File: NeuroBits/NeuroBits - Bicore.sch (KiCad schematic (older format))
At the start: 8 parts, among them IC1 NL17SZ14DBVT1G, IC2 NL17SZ14DBVT1G, J1 Conn_01x04_Female

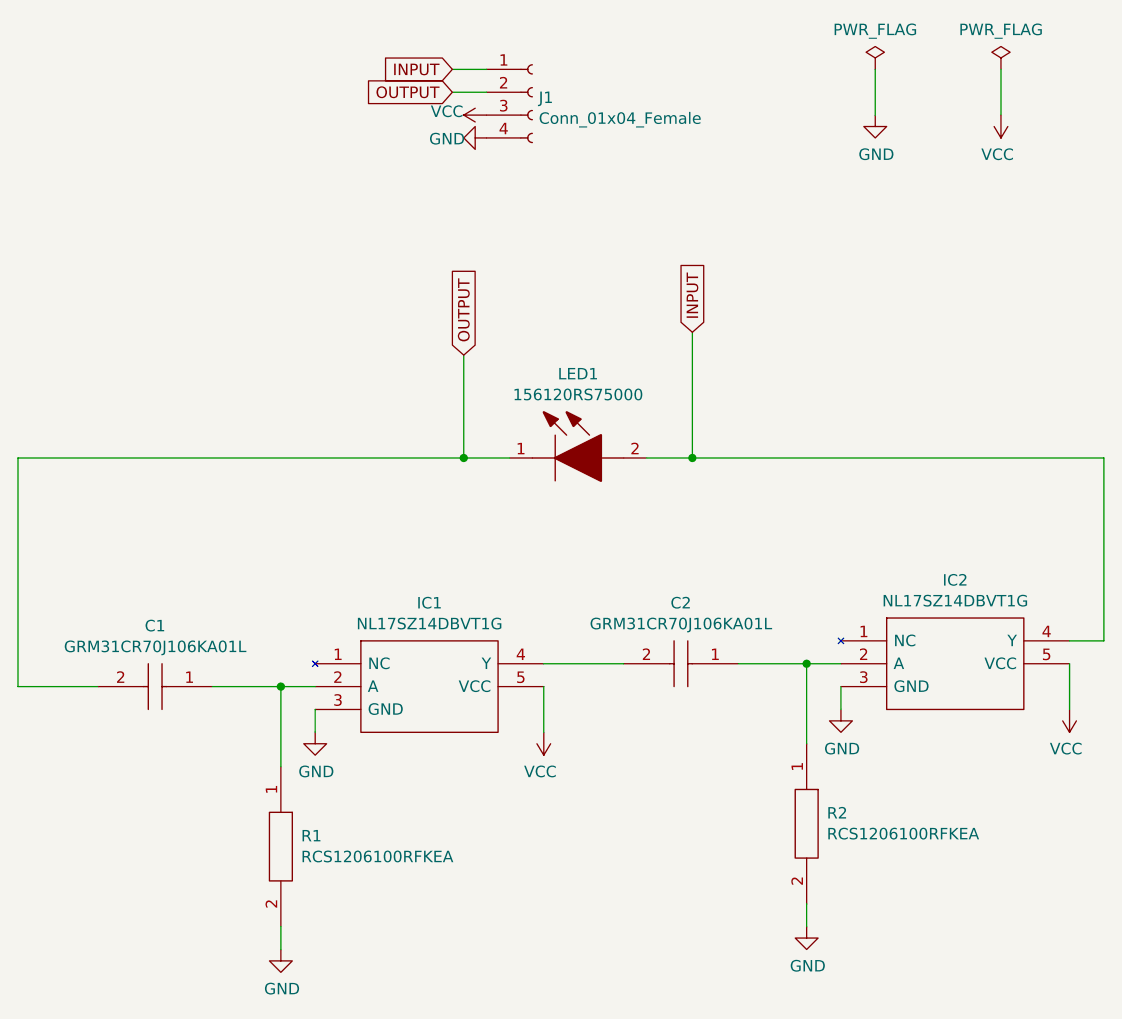
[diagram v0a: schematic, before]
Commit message: added BioRuler initial commit
added project for a custom STM32 based solar powered ultracapacitor microcontroller for biological research
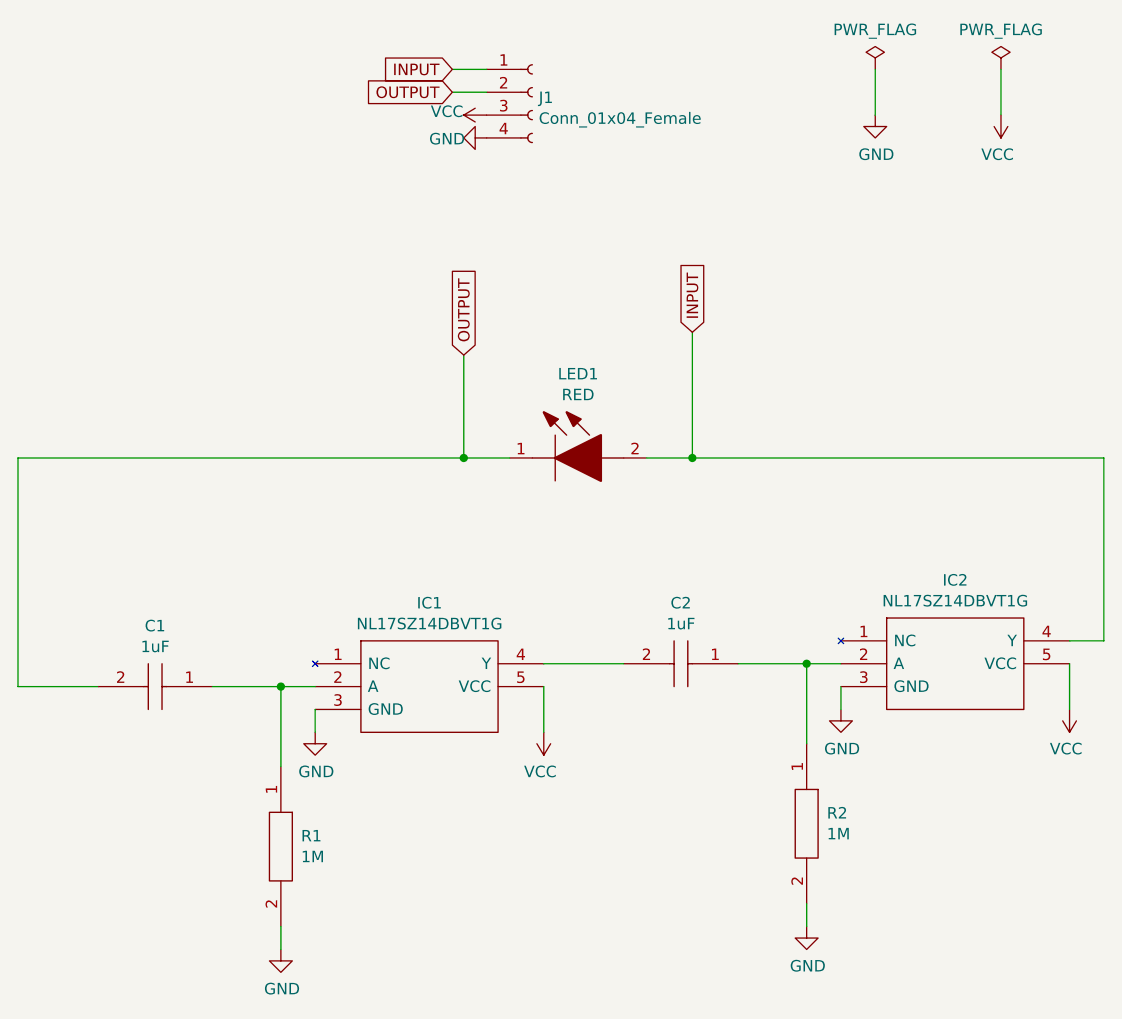
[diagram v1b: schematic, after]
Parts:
- C1, C2: value GRM31CR70J106KA01L -> 1uF
- LED1: value 156120RS75000 -> RED
- R1, R2: value RCS1206100RFKEA -> 1M
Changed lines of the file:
@@
 P 4600 4450
 F 0 "R1" V 4904 4538 50  0000 L CNN
-F 1 "RCS1206100RFKEA" V 4995 4538 50  0000 L CNN
+F 1 "1M" V 4995 4538 50  0000 L CNN
 F 2 "RESC3216X65N" H 5150 4500 50  0001 L CNN
 F 3 "https://www.vishay.com/docs/20065/rcse3.pdf" H 5150 4400 50  0001 L CNN
@@
 P 4300 4100
 F 0 "C1" H 4550 3835 50  0000 C CNN
-F 1 "GRM31CR70J106KA01L" H 4550 3926 50  0000 C CNN
+F 1 "1uF" H 4550 3926 50  0000 C CNN
 F 2 "CAPC3216X180N" H 4650 4150 50  0001 L CNN
 F 3 "http://www.murata.com/~/media/webrenewal/support/library/catalog/products/capacitor/mlcc/c02e.pdf" H 4650 4050 50  0001 L CNN
@@
 P 6900 4350
 F 0 "R2" V 7204 4438 50  0000 L CNN
-F 1 "RCS1206100RFKEA" V 7295 4438 50  0000 L CNN
+F 1 "1M" V 7295 4438 50  0000 L CNN
 F 2 "RESC3216X65N" H 7450 4400 50  0001 L CNN
 F 3 "https://www.vishay.com/docs/20065/rcse3.pdf" H 7450 4300 50  0001 L CNN
@@
 P 6600 4000
 F 0 "C2" H 6850 3735 50  0000 C CNN
-F 1 "GRM31CR70J106KA01L" H 6850 3826 50  0000 C CNN
+F 1 "1uF" H 6850 3826 50  0000 C CNN
 F 2 "CAPC3216X180N" H 6950 4050 50  0001 L CNN
 F 3 "http://www.murata.com/~/media/webrenewal/support/library/catalog/products/capacitor/mlcc/c02e.pdf" H 6950 3950 50  0001 L CNN
@@
 P 5600 3100
 F 0 "LED1" H 5900 3467 50  0000 C CNN
-F 1 "156120RS75000" H 5900 3376 50  0000 C CNN
+F 1 "RED" H 5900 3376 50  0000 C CNN
 F 2 "LEDM3216X130N" H 6100 3250 50  0001 L BNN
 F 3 "https://katalog.we-online.com/led/datasheet/156120RS75000.pdf" H 6100 3150 50  0001 L BNN
